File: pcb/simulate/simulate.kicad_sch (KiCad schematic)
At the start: 15 parts, among them U1 ${SIM.PARAMS}, U2 ${SIM.PARAMS}

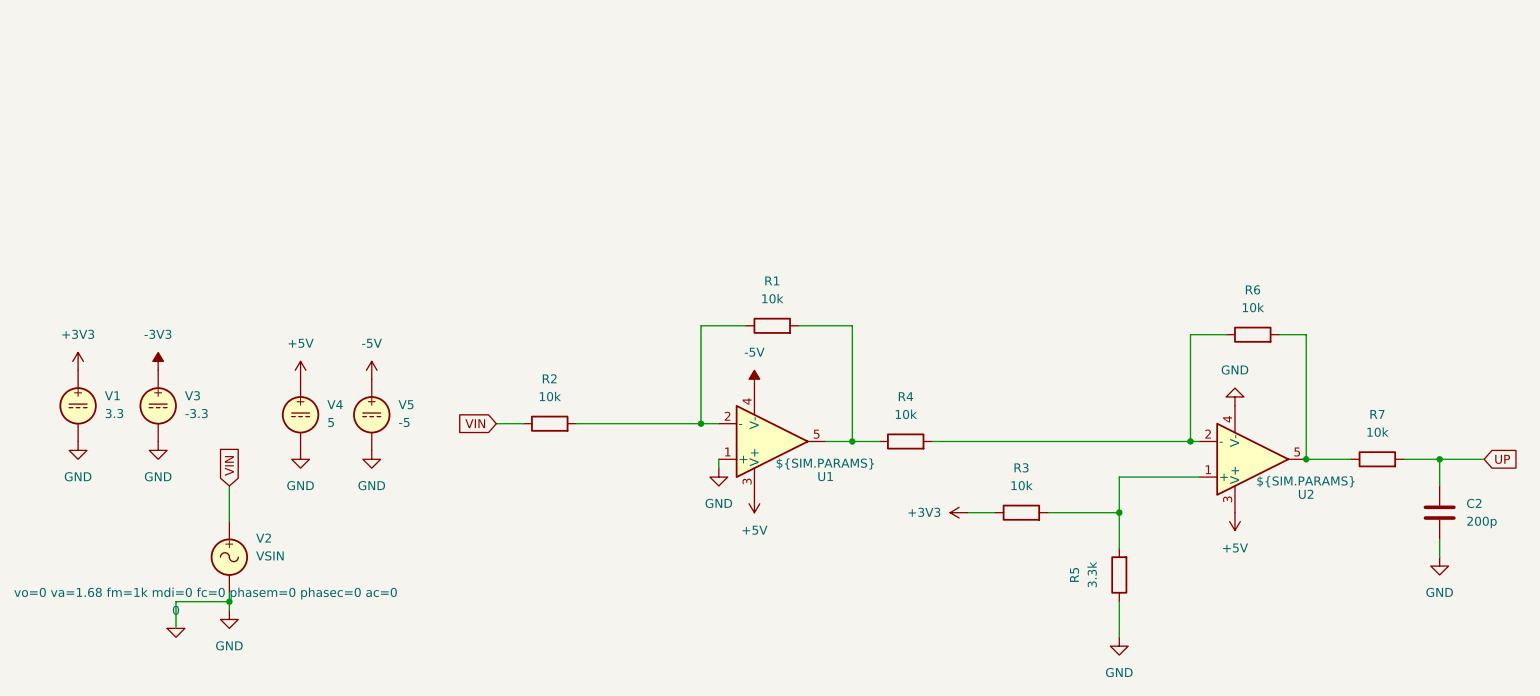
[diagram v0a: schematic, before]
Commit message: Update simulation waveform colors and add NJM2747D symbol library
- Changed the waveform color for the input voltage (VIN) to a new RGB value.
- Updated the waveform color for the output voltage (VOUT) to a different RGB value.
- Added cursor formatting for both VIN and VOUT signals in the simulation.
- Introduced a new symbol library for the NJM2747D component in the project.
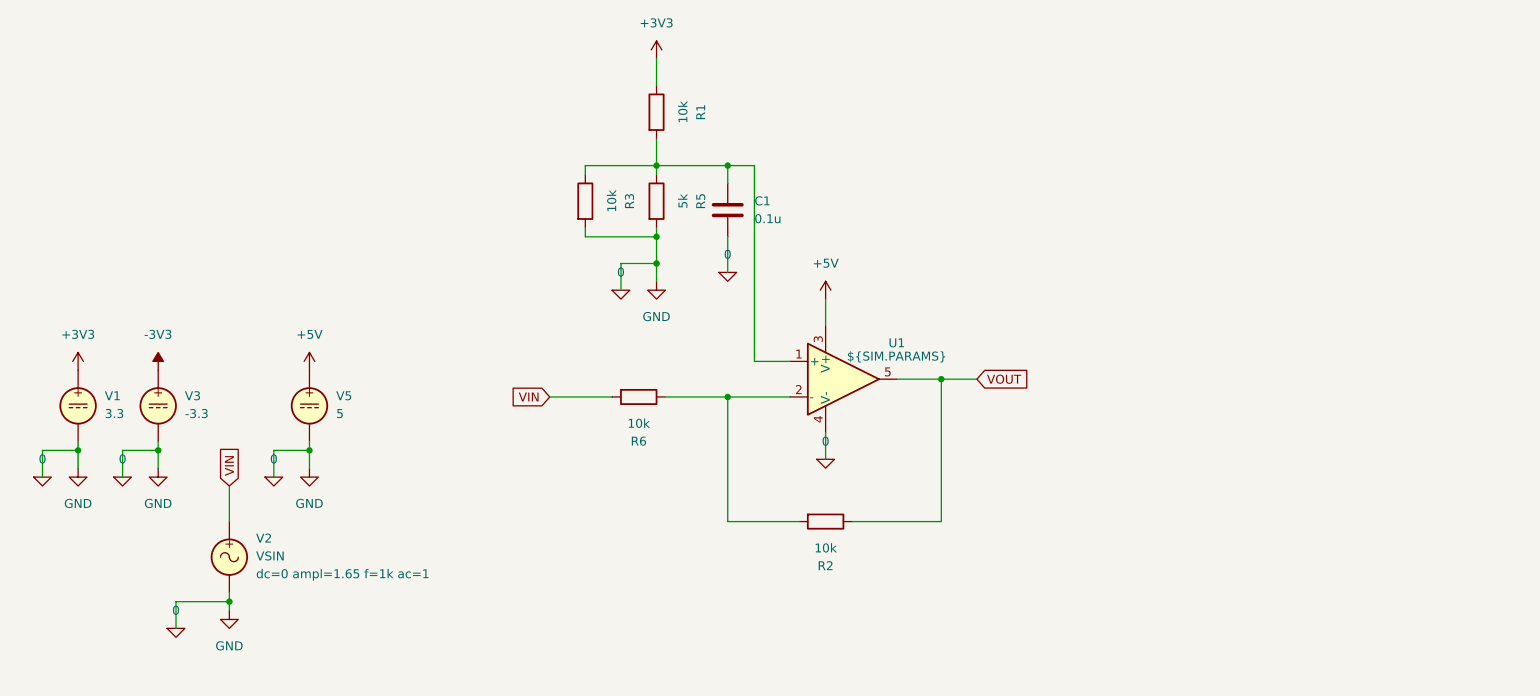
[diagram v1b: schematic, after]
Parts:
- removed C2: 200p, symbol Device:C
- removed R4, R7: 10k, symbol Device:R
- removed U2: ${SIM.PARAMS}, symbol Simulation_SPICE:OPAMP
- removed V4: 5, symbol Simulation_SPICE:VDC
- added C1: 0.1u, symbol Device:C
- R5: value 3.3k -> 5k
- V5: value -5 -> 5
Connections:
- net +3V3: now also R1.1; no longer R3.1
- net +5V: now also V5.1
- net 0: now also R3.2, R5.2, U1.4 (V-), C1.2; no longer R5.1, U1.1 (+)
- net VIN: now also R6.2; no longer R2.1
- net at R2.2, U1.2 (-): now also R6.1; no longer R1.1
- net at R1.2: now also R3.1, R5.1, U1.1 (+), C1.1; no longer U1.5
- removed net -5V: U1.4 (V-), V5.1
- new net VOUT: R2.1, U1.5
